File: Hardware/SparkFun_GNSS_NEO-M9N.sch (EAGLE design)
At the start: 45 parts, among them J1 MICROMOD_STANDARD, U1 U-BLOX_NEO-M9N, U2 3.3V, U3 EEPROM

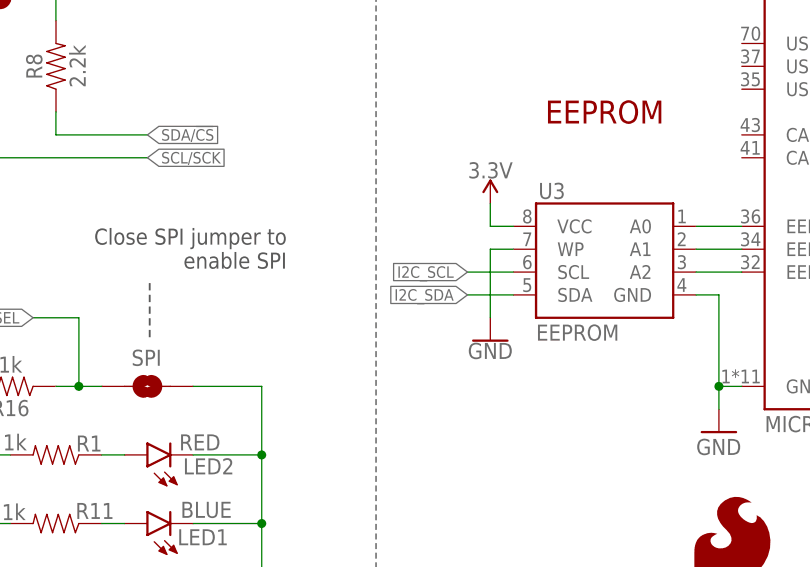
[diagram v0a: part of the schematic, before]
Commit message: Correctly routes I2C to EEPROM chip
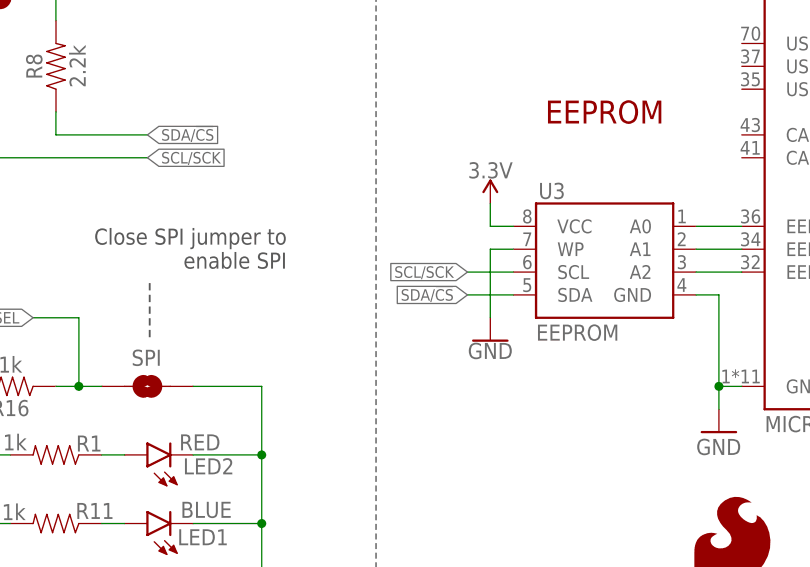
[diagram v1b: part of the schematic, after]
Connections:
- removed net I2C_SCL: U3.SCL
- removed net I2C_SDA: U3.SDA
- net SCL/SCK: now also U3.SCL
- net SDA/!CS: now also U3.SDA
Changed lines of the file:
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@@
 <pinref part="J1" gate="J1" pin="I2C_SCL"/>
+</segment>
+<segment>
+<pinref part="U3" gate="G$1" pin="SCL"/>
+<wire x1="78.74" y1="48.26" x2="73.66" y2="48.26" width="0.1524" layer="91"/>
+<label x="73.66" y="48.26" size="1.27" layer="95" rot="R180" xref="yes"/>
 </segment>
 </net>
@@
 <label x="142.24" y="76.2" size="1.27" layer="95" font="vector" xref="yes"/>
 <pinref part="J1" gate="J1" pin="I2C_SDA"/>
+</segment>
+<segment>
+<pinref part="U3" gate="G$1" pin="SDA"/>
+<wire x1="78.74" y1="45.72" x2="73.66" y2="45.72" width="0.1524" layer="91"/>
+<label x="73.66" y="45.72" size="1.27" layer="95" rot="R180" xref="yes"/>
 </segment>
 </net>
@@
 </segment>
 </net>
-<net name="I2C_SCL" class="0">
-<segment>
-<pinref part="U3" gate="G$1" pin="SCL"/>
-<wire x1="78.74" y1="48.26" x2="73.66" y2="48.26" width="0.1524" layer="91"/>
-<label x="73.66" y="48.26" size="1.27" layer="95" rot="R180" xref="yes"/>
-</segment>
-</net>
-<net name="I2C_SDA" class="0">
-<segment>
-<pinref part="U3" gate="G$1" pin="SDA"/>
-<wire x1="78.74" y1="45.72" x2="73.66" y2="45.72" width="0.1524" layer="91"/>
-<label x="73.66" y="45.72" size="1.27" layer="95" rot="R180" xref="yes"/>
-</segment>
-</net>

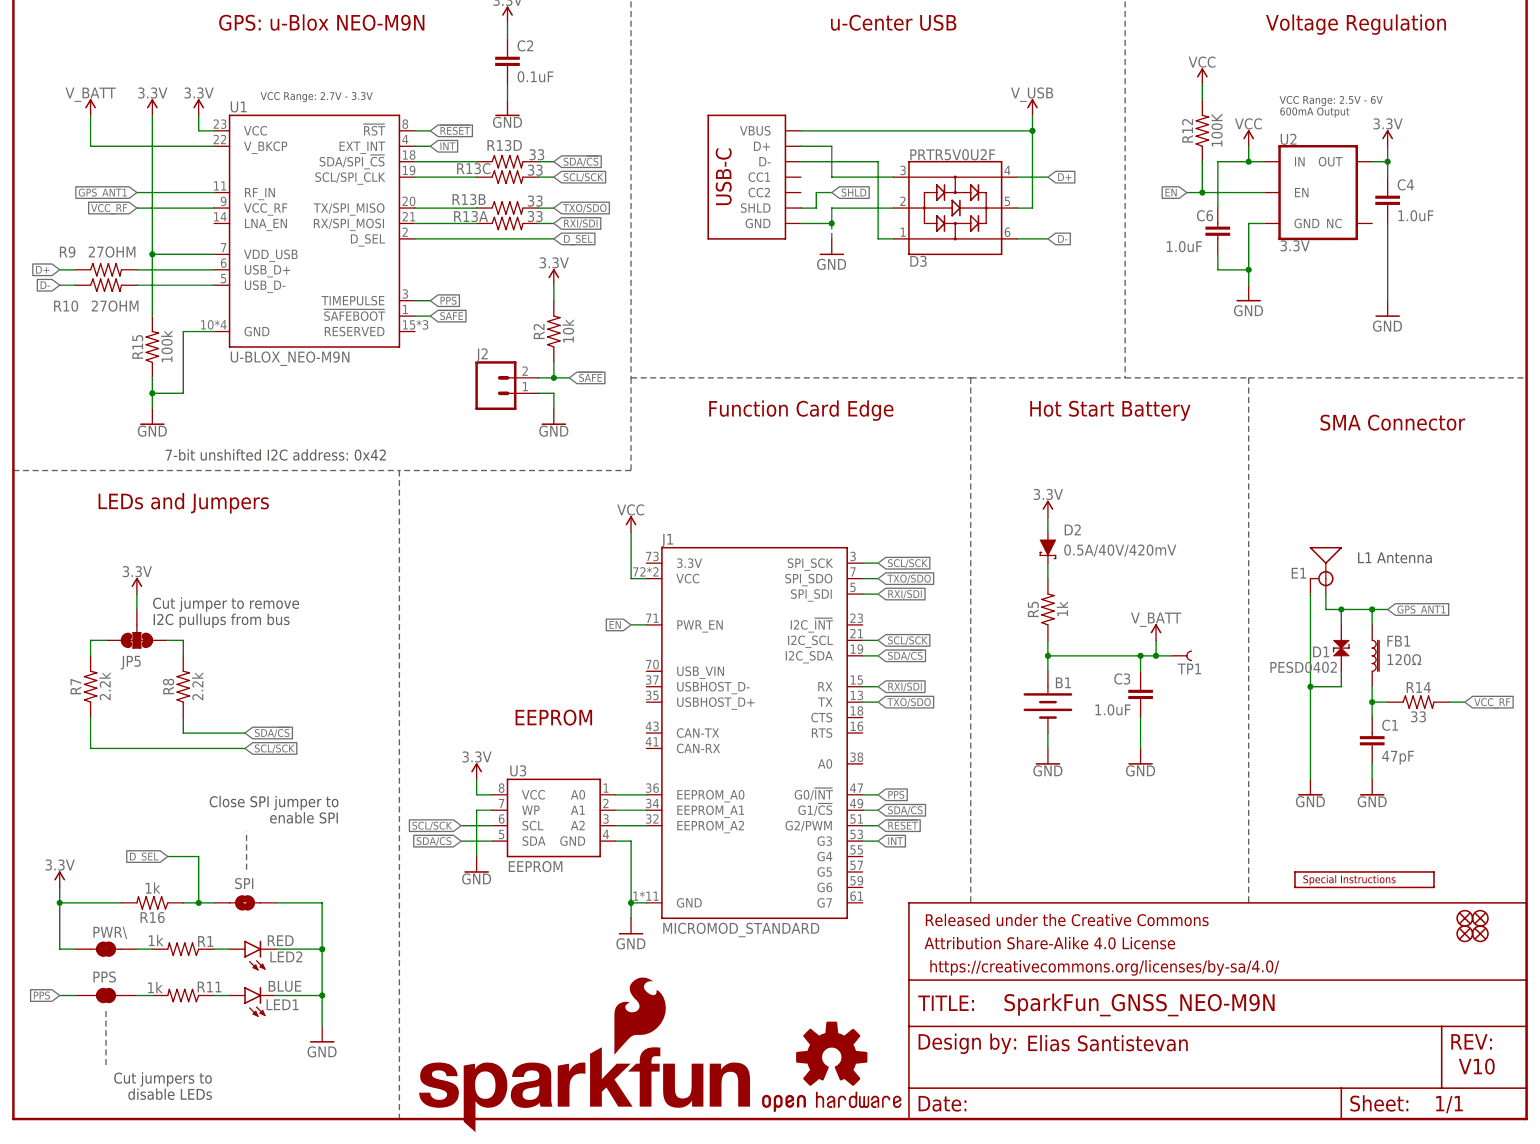
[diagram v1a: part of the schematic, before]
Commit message: Moves to 0603 components where they can be, updates measures
* Moves around vias for symmetrical appeal (though I burned out and so it's not)
* Adds silk
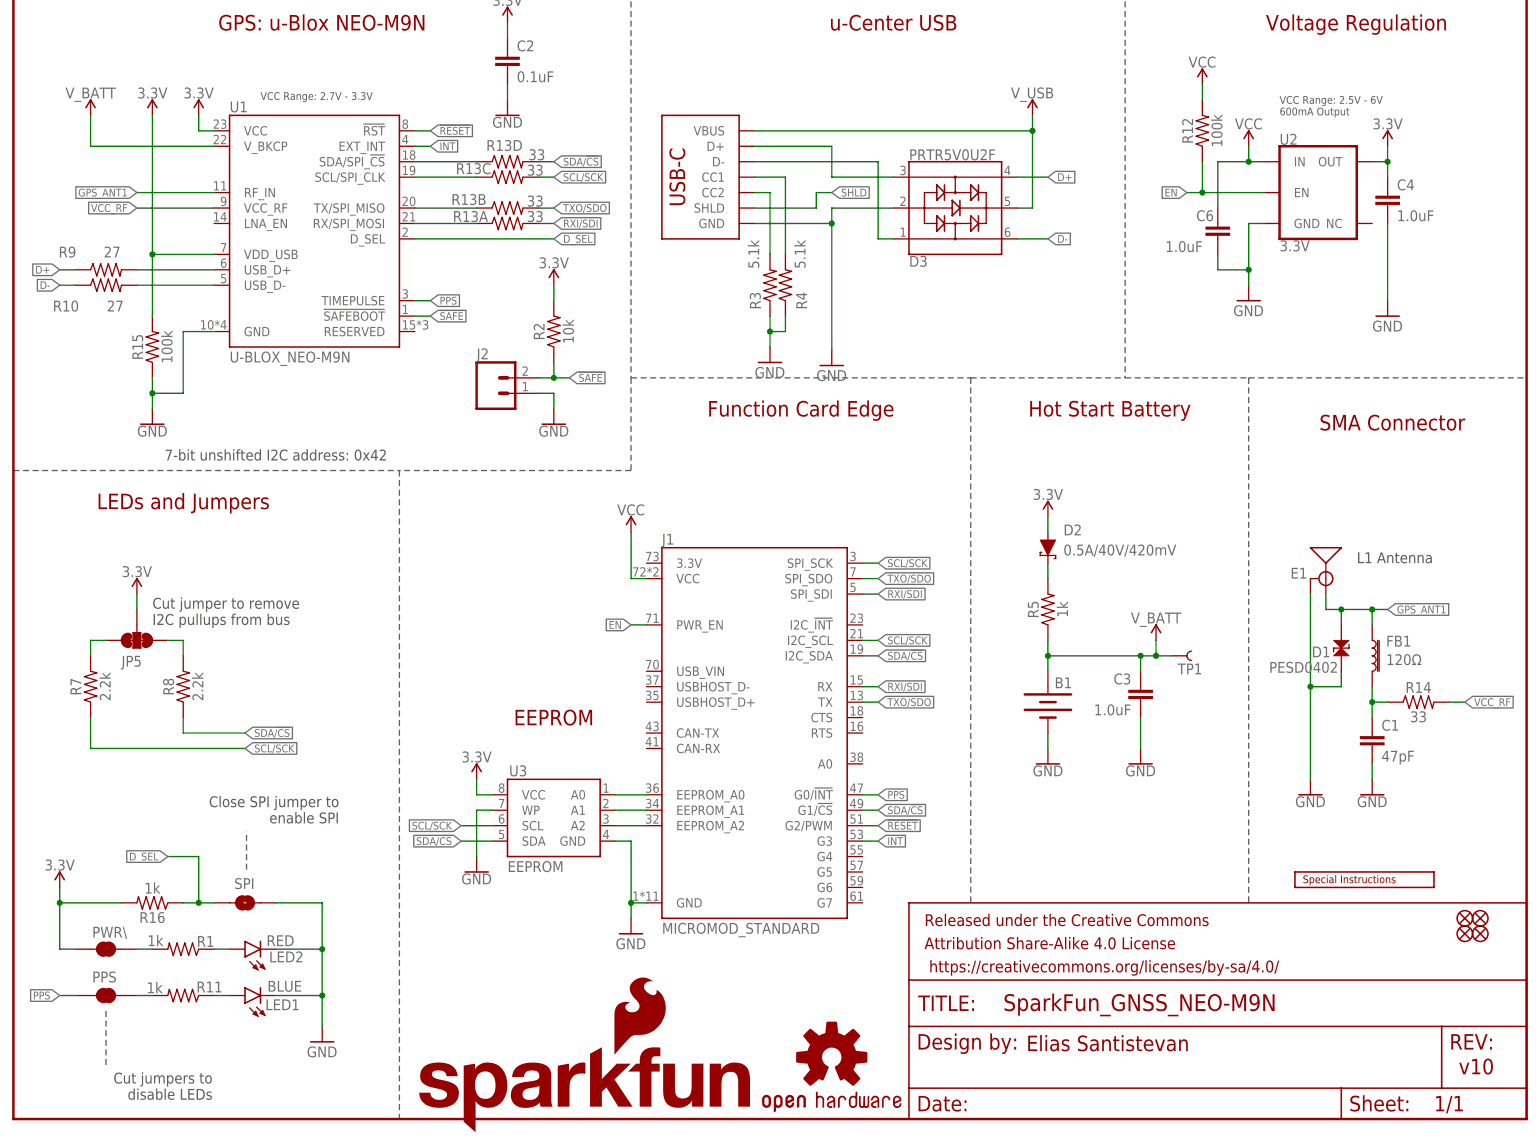
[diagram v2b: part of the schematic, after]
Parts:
- added R3, R4: 5.1k, SparkFun-Resistors:5.1KOHM5.1KOHM-0603-1/10W-1%
- C3, C4, C6: device SparkFun-Capacitors:1.0UF-0402T-16V-10% -> SparkFun-Capacitors:1.0UF-0603-16V-10%
- R1, R11, R16, R5: device SparkFun-Resistors:1KOHM-0402T-1/16W-1% -> SparkFun-Resistors:1KOHM-0603-1/10W-1%
- R10, R9: value 27OHM -> 27; device SparkFun-Resistors:27OHM -> SparkFun-Resistors:27OHM-0603-1/10W-1%
- R12: value 100K -> 100k; device SparkFun-Resistors:100KOHM-0402-1/16W-1% -> SparkFun-Resistors:100KOHM-0603-1/10W-1%
- R15: device SparkFun-Resistors:100KOHM-0402T-1/16W-1% -> SparkFun-Resistors:100KOHM-0603-1/10W-1%
- R2: device SparkFun-Resistors:10KOHM-0402-1/16W-1% -> SparkFun-Resistors:10KOHM-0603-1/10W-1%
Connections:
- new net N$7: J3.CC1, R4.2
- new net N$9: J3.CC2, R3.2
- net GND: now also R3.1, R4.1
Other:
- note added: "v10"
- note removed: "V10"

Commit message: Routes new switching ICs
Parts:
- removed FRAME1: FRAME-LETTER, SparkFun-Aesthetics:FRAME-LETTER
- removed R16: 1k, SparkFun-Resistors:1KOHM-0603-1/10W-1%
- removed SPI: JUMPER-SMT_2_NO_SILK, SparkFun-Jumpers:JUMPER-SMT_2_NO_SILK
- added C5, C7: 0.1uF, SparkFun-Capacitors:0.1UF-0603-25V-(+80/-20%)
- added FRAME2: FRAME-LEDGER, SparkFun-Aesthetics:FRAME-LEDGER
- added J4: (no value), SparkFun-Connectors:CONN_03LOCK
- added R6: 10k, SparkFun-Resistors:10KOHM-0603-1/10W-1%
- added U$15, U$8: 74LVC4066D_QUAD_BILATERAL_SWITCH, SparkFun-IC-Logic:74LVC4066D_QUAD_BILATERAL_SWITCH
- added U4: 74HC1G04, SparkFun-IC-Logic:74HC1G04
- R7, R8: value 2.2k -> 4.7k; device SparkFun-Resistors:2.2KOHM-0603-1/10W-1% -> SparkFun-Resistors:4.7KOHM-0603-1/10W-1%
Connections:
- removed net SDA/!CS: J1.G1/!CS!, J1.I2C_SDA, R13D.2, R8.1, U3.SDA
- new net INV_D_SEL: U$15.1E, U$15.2E, U$15.3E, U$15.4E, U4G1.Y
- new net N$13: J4.1, R6.1
- new net RXI: J1.RX, U$8.4Z
- new net SCK: J1.SPI_SCK, U$15.2Z
- new net SCL: J1.I2C_SCL, R7.1, U$8.2Z, U3.SCL
- new net SDA: J1.I2C_SDA, R8.1, U$8.1Z, U3.SDA
- new net SDA/SPI_!CS!: R13D.2, U$15.1Y, U$8.1Y
- new net SDI: J1.SPI_SDI, U$15.4Z
- new net SDO: J1.SPI_SDO, U$15.3Z
- new net SPI_!CS!: J1.G1/!CS!, U$15.1Z
- new net TXO: J1.TX, U$8.3Z
- net 3.3V: now also C5.1, C7.1, R6.2, U$15.VCC, U$8.VCC, U4G2.P$V+; no longer R16.2
- net D_SEL: now also J4.2, U$8.1E, U$8.2E, U$8.3E, U$8.4E, U4G1.A; no longer R16.1, SPI.2
- net GND: now also C5.2, C7.2, J4.3, U$15.GND, U$8.GND, U4G2.P$V-; no longer SPI.1
- net RXI/SDI: now also U$15.4Y, U$8.4Y; no longer J1.RX, J1.SPI_SDI
- net SCL/SCK: now also U$15.2Y, U$8.2Y; no longer J1.I2C_SCL, J1.SPI_SCK, R7.1, U3.SCL
- net TXO/SDO: now also U$15.3Y, U$8.3Y; no longer J1.SPI_SDO, J1.TX
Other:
- note removed: "Close SPI jumper to enable SPI"
- moved on the sheet: B1, C1, C2, C3, C4, C6, D1, D2, D3, E1, FB1, J1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

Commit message: Moves silk around, seeds new vias around the PCB
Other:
- note added: "Bus Selection: 74LVC4066D"
- note added: "SPI or I2C+Serial Selection"
- note added: "To use SPI simply move the shunt to the side labeled "SPI"."
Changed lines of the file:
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@@
 <wire x1="261.62" y1="0" x2="261.62" y2="93.98" width="0.2032" layer="97" style="longdash"/>
 <wire x1="198.12" y1="0" x2="198.12" y2="93.98" width="0.2032" layer="97" style="longdash"/>
+<text x="256.54" y="182.88" size="2.54" layer="94" font="vector">Bus Selection: 74LVC4066D</text>
+<text x="320.04" y="116.84" size="1.778" layer="97" font="vector">To use SPI simply
+move the shunt to the side labeled
+"SPI".</text>
+<text x="261.62" y="177.8" size="1.778" layer="97" font="vector">SPI or I2C+Serial Selection</text>
 </plain>
 <instances>

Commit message: Adds more text to clarify selection jumper, fixes some clearance issues and wire stubs
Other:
- note added: "Default is I2C and Serial"
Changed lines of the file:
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@@
 <wire x1="198.12" y1="0" x2="198.12" y2="93.98" width="0.2032" layer="97" style="longdash"/>
 <text x="256.54" y="182.88" size="2.54" layer="94" font="vector">Bus Selection: 74LVC4066D</text>
-<text x="320.04" y="116.84" size="1.778" layer="97" font="vector">To use SPI simply
+<text x="320.04" y="119.38" size="1.778" layer="97" font="vector">To use SPI simply
 move the shunt to the side labeled
 "SPI".</text>
 <text x="261.62" y="177.8" size="1.778" layer="97" font="vector">SPI or I2C+Serial Selection</text>
+<text x="320.04" y="111.76" size="1.778" layer="97" font="vector">Default is I2C and Serial</text>
+<wire x1="340.36" y1="116.84" x2="370.84" y2="116.84" width="0.2032" layer="97"/>
+<wire x1="370.84" y1="116.84" x2="368.3" y2="119.38" width="0.2032" layer="97"/>
+<wire x1="370.84" y1="116.84" x2="368.3" y2="114.3" width="0.2032" layer="97"/>
+<wire x1="340.36" y1="119.38" x2="340.36" y2="116.84" width="0.2032" layer="97"/>
+<wire x1="340.36" y1="116.84" x2="340.36" y2="114.3" width="0.2032" layer="97"/>
 </plain>
 <instances>

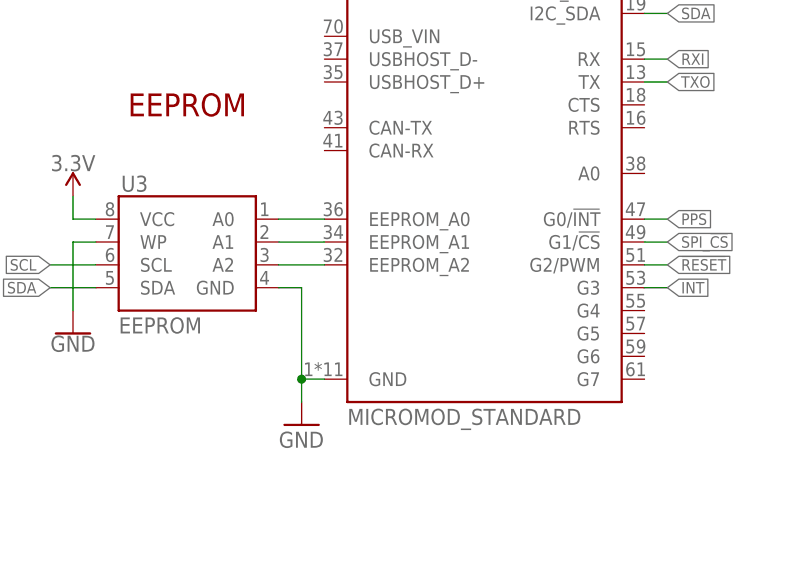
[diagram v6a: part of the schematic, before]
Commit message: Adds WP pin to schematic
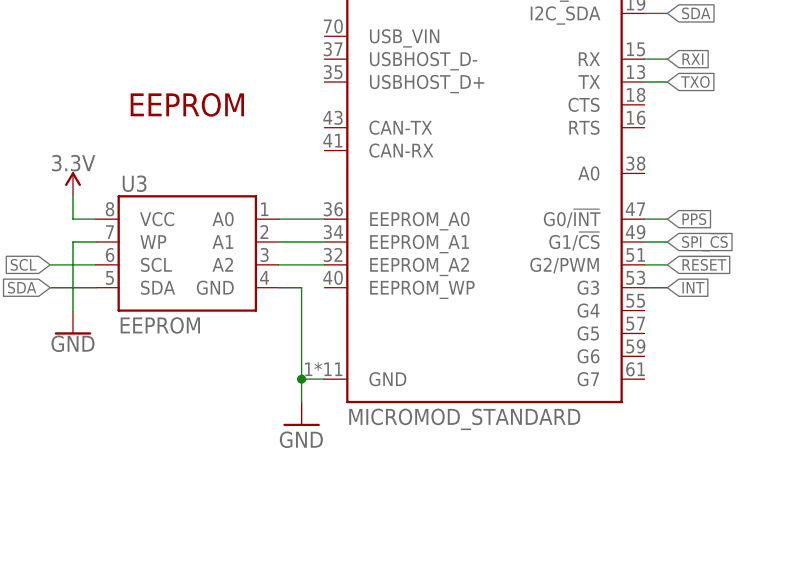
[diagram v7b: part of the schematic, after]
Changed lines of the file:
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@@
 <?xml version="1.0" encoding="utf-8"?>
 <!DOCTYPE eagle SYSTEM "eagle.dtd">
-<eagle version="9.5.1">
+<eagle version="9.6.2">
 <drawing>
 <settings>

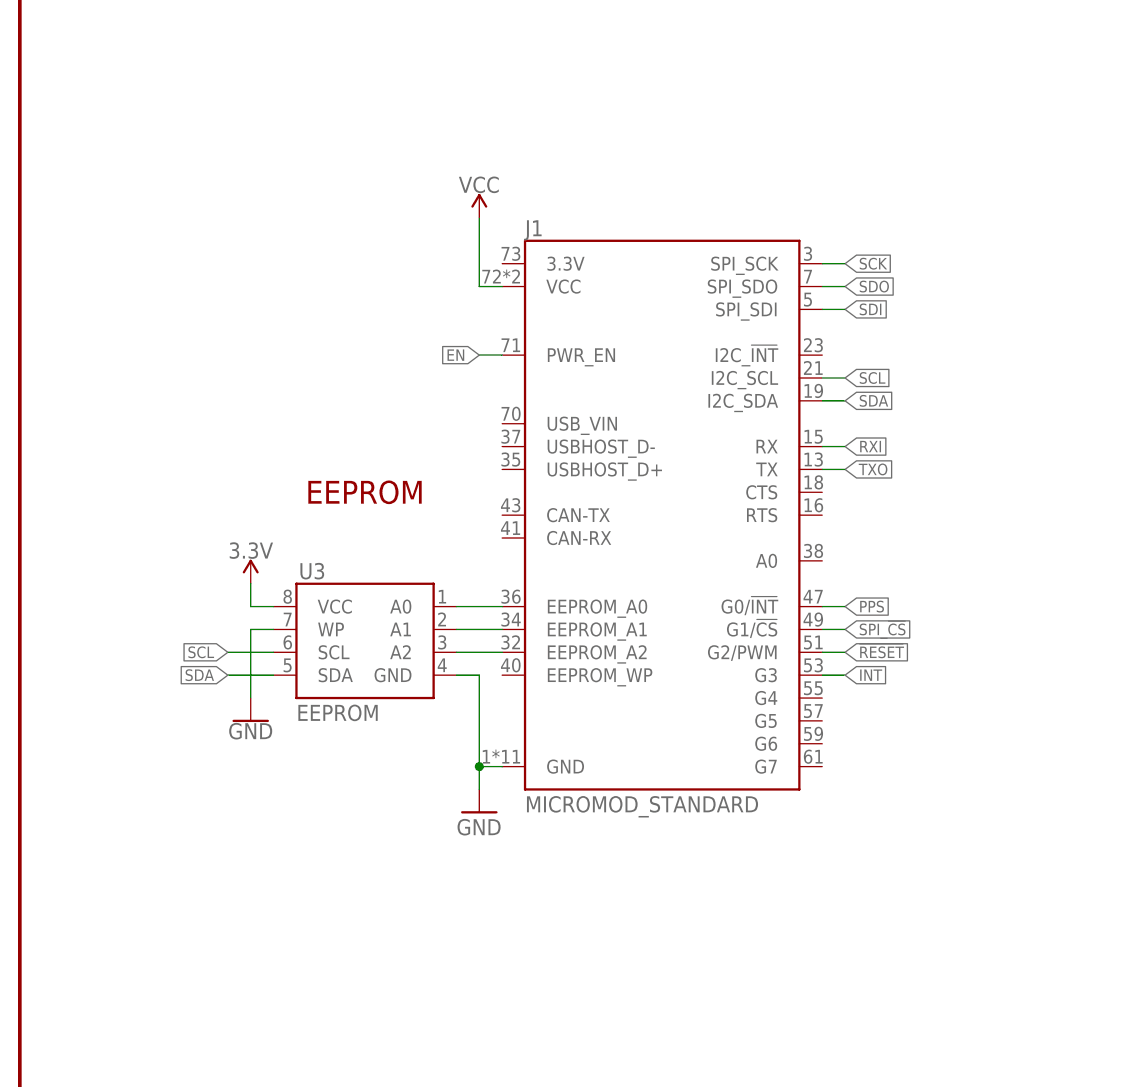
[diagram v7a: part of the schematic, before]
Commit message: Loosely adds placement of WP circuit to PCB
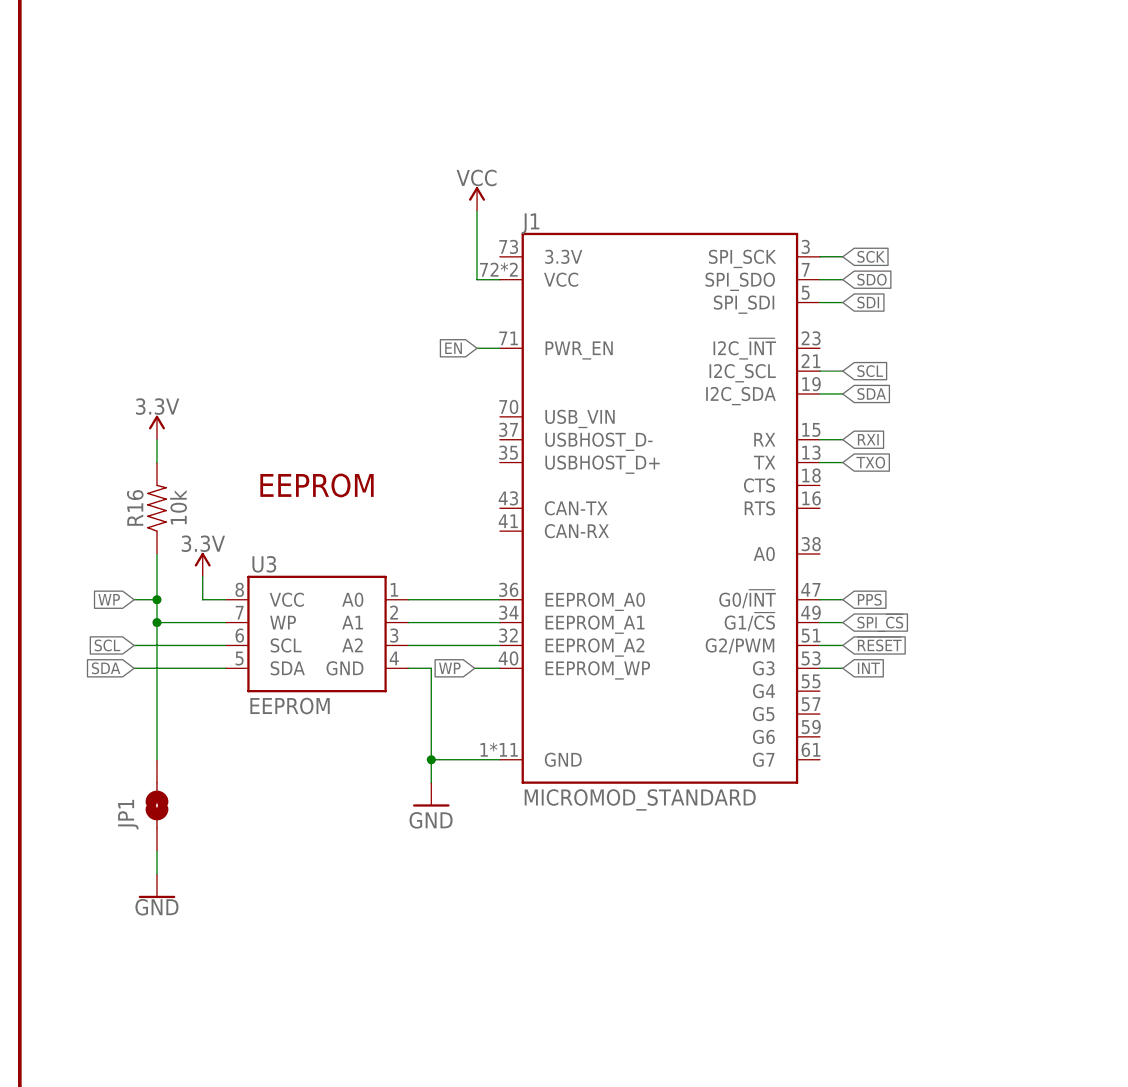
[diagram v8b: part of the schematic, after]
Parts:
- added JP1: JUMPER-SMT_2_NO_SILK, SparkFun-Jumpers:JUMPER-SMT_2_NO_SILK
- added R16: 10k, SparkFun-Resistors:10KOHM-0603-1/10W-1%
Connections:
- new net WP: J1.EEPROM_WP, JP1.2, R16.1, U3.WP
- net 3.3V: now also R16.2
- net GND: now also JP1.1; no longer U3.WP
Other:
- moved on the sheet: J1, U3
